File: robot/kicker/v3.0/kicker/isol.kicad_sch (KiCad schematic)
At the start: 11 parts, among them J4 Conn_01x10, U6 ISO6720-Q1, U7 ISO6720-Q1, U8 ISO6721-Q1

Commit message: kicker v3.0 digital schematic work
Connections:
- net GND_ISOL: now also R51.1; no longer R51.2
- net ~{DET}: now also R51.2; no longer R51.1
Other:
- note removed: "This power management IC is isolated from HV side."
- moved on the sheet: C, C43, C44, C45, C46, C47, J4, R51, U6, U7, U8

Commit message: lots of ERC work
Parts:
- renumbered C to C28, C43 to C29, C44 to C30, C45 to C31, C46 to C32, C47 to C33, R51 to R49, U6 to U9
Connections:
- net BOOT0 renamed MCU_BOOT_UART.BOOT0
- net PWR_EN renamed MCU_BOOT_UART.PWR_EN
- net RX renamed MCU_BOOT_UART.RX
- net TX renamed MCU_BOOT_UART.TX
- net ~{DET} renamed MCU_BOOT_UART.~{DET}
- net ~{RST} renamed MCU_BOOT_UART.~{RST}
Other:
- moved on the sheet: C28, C29, C30, C31, C32, C33, R49, U7, U8, U9

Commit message: kicker v3.0 passing ERC
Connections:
- net CLK_8M.CLK_n renamed 32KHZ_CLK_REF
- net CLK_8M.CLK_p renamed 8MHZ_CLK_REF
- net CLK_8M_ISOLn renamed CLK_32K_ISOL
- net CLK_8M_ISOLp renamed CLK_8M_ISOL
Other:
- company: (none) -> SSL A-Team
- title: (none) -> Kicker v3.0
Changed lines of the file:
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@@
 (kicad_sch (version 20230121) (generator eeschema)
   (paper "A4")
+  (title_block
+    (title "Kicker v3.0")
+    (date "2023-11-07")
+    (rev "0")
+    (company "SSL A-Team")
+    (comment 1 "Author: William Stuckey")
+  )
   (junction (at 223.52 113.03) (diameter 0) (color 0 0 0 0)
   )
@@
   (junction (at 173.99 113.03) (diameter 0) (color 0 0 0 0)
   )
+  (bus_entry (at 248.92 127) (size -2.54 2.54)
+    (stroke (width 0) (type default))
+  )
+  (bus_entry (at 111.76 53.34) (size -2.54 2.54)
+    (stroke (width 0) (type default))
+  )
+  (bus_entry (at 248.92 129.54) (size -2.54 2.54)
+    (stroke (width 0) (type default))
+  )
+  (bus_entry (at 248.92 83.82) (size -2.54 2.54)
+    (stroke (width 0) (type default))
+  )
+  (bus_entry (at 248.92 86.36) (size -2.54 2.54)
+    (stroke (width 0) (type default))
+  )
+  (bus_entry (at 247.65 43.18) (size -2.54 2.54)
+    (stroke (width 0) (type default))
+  )
+  (bus_entry (at 111.76 55.88) (size -2.54 2.54)
+    (stroke (width 0) (type default))
+  )
+  (bus_entry (at 111.76 55.88) (size -2.54 2.54)
+    (stroke (width 0) (type default))
+  )
   (bus_entry (at 247.65 45.72) (size -2.54 2.54)
     (stroke (width 0) (type default))
   )
-  (bus_entry (at 248.92 127) (size -2.54 2.54)
-    (stroke (width 0) (type default))
-  )
-  (bus_entry (at 111.76 53.34) (size -2.54 2.54)
-    (stroke (width 0) (type default))
-  )
-  (bus_entry (at 248.92 129.54) (size -2.54 2.54)
-    (stroke (width 0) (type default))
-  )
-  (bus_entry (at 248.92 83.82) (size -2.54 2.54)
-    (stroke (width 0) (type default))
-  )
-  (bus_entry (at 248.92 86.36) (size -2.54 2.54)
-    (stroke (width 0) (type default))
-  )
-  (bus_entry (at 111.76 55.88) (size -2.54 2.54)
-    (stroke (width 0) (type default))
-  )
-  (bus_entry (at 247.65 43.18) (size -2.54 2.54)
-    (stroke (width 0) (type default))
-  )
-  (bus_entry (at 111.76 55.88) (size -2.54 2.54)
-    (stroke (width 0) (type default))
-  )
   (wire (pts (xy 100.33 55.88) (xy 109.22 55.88))
     (stroke (width 0) (type default))
@@
     (effects (font (size 1.27 1.27)) (justify left bottom))
   )
-  (label "CLK_8M_ISOLn" (at 52.07 63.5 0) (fields_autoplaced)
+  (label "CLK_32K_ISOL" (at 52.07 63.5 0) (fields_autoplaced)
     (effects (font (size 1.27 1.27)) (justify left bottom))
   )
@@
     (effects (font (size 1.27 1.27)) (justify left bottom))
   )
-  (label "CLK_8M.CLK_n" (at 215.9 48.26 0) (fields_autoplaced)
-    (effects (font (size 1.27 1.27)) (justify left bottom))
-  )
-  (label "CLK_8M_ISOLp" (at 182.88 45.72 180) (fields_autoplaced)
+  (label "CLK_8M_ISOL" (at 182.88 45.72 180) (fields_autoplaced)
     (effects (font (size 1.27 1.27)) (justify right bottom))
   )
@@
     (effects (font (size 1.27 1.27)) (justify left bottom))
   )
-  (label "MCU_BOOT_UART.PWR_EN" (at 71.12 58.42 0)
+  (label "32KHZ_CLK_REF" (at 217.17 48.26 0)
+    (effects (font (size 1.27 1.27)) (justify left bottom))
+  )
+  (label "MCU_BOOT_UART.PWR_EN" (at 71.12 58.42 0) (fields_autoplaced)
     (effects (font (size 1.27 1.27)) (justify left bottom))
   )
@@
     (effects (font (size 1.27 1.27)) (justify right bottom))
   )
-  (label "CLK_8M.CLK_p" (at 215.9 45.72 0) (fields_autoplaced)
-    (effects (font (size 1.27 1.27)) (justify left bottom))
-  )
   (label "MCU_BOOT_UART.TX" (at 215.9 88.9 0) (fields_autoplaced)
     (effects (font (size 1.27 1.27)) (justify left bottom))
@@
     (effects (font (size 1.27 1.27)) (justify left bottom))
   )
+  (label "8MHZ_CLK_REF" (at 217.17 45.72 0)
+    (effects (font (size 1.27 1.27)) (justify left bottom))
+  )
   (label "BOOT_UART_TX_ISOL" (at 182.88 88.9 180) (fields_autoplaced)
     (effects (font (size 1.27 1.27)) (justify right bottom))
@@
     (effects (font (size 1.27 1.27)) (justify left bottom))
   )
-  (label "CLK_8M_ISOLn" (at 182.88 48.26 180) (fields_autoplaced)
+  (label "CLK_32K_ISOL" (at 182.88 48.26 180) (fields_autoplaced)
     (effects (font (size 1.27 1.27)) (justify right bottom))
   )
@@
     (effects (font (size 1.27 1.27)) (justify left bottom))
   )
-  (label "CLK_8M_ISOLp" (at 52.07 60.96 0) (fields_autoplaced)
-    (effects (font (size 1.27 1.27)) (justify left bottom))
-  )
-  (label "MCU_BOOT_UART.~{RST}" (at 214.63 132.08 0)
+  (label "CLK_8M_ISOL" (at 52.07 60.96 0) (fields_autoplaced)
+    (effects (font (size 1.27 1.27)) (justify left bottom))
+  )
+  (label "MCU_BOOT_UART.~{RST}" (at 214.63 132.08 0) (fields_autoplaced)
     (effects (font (size 1.27 1.27)) (justify left bottom))
   )
@@
     (effects (font (size 1.27 1.27)) (justify left))
   )
-  (hierarchical_label "CLK_8M{DCLK}" (shape output) (at 251.46 39.37 0) (fields_autoplaced)
+  (hierarchical_label "{SYSCLK}" (shape output) (at 251.46 39.37 0) (fields_autoplaced)
     (effects (font (size 1.27 1.27)) (justify left))
   )

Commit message: footprint work
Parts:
- C28, C29, C30, C31, C32, C33: value 100n -> 100n 6.3V
- J4: footprint (none) -> Connector_JST:JST_SH_SM10B-SRSS-TB_1x10-1MP_P1.00mm_Horizontal
- R49: footprint (none) -> Resistor_SMD:R_0402_1005Metric
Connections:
- net GND: now also C31.2, C32.2, C33.2
- net GND_ISOL: no longer C31.2, C32.2, C33.2
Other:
- moved on the sheet: C28, C29, C30, C31, C32, C33

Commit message: kicker v3.0 footprint work
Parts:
- C28, C29, C30, C31, C32, C33: footprint (none) -> Capacitor_SMD:C_0402_1005Metric
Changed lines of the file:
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@@
       (effects (font (size 1.27 1.27)) (justify left))
     )
-    (property "Footprint" "" (at 171.45 74.93 0)
+    (property "Footprint" "Capacitor_SMD:C_0402_1005Metric" (at 171.45 74.93 0)
       (effects (font (size 1.27 1.27)) hide)
     )
@@
       (effects (font (size 1.27 1.27)) (justify left))
     )
-    (property "Footprint" "" (at 226.06 72.39 0)
+    (property "Footprint" "Capacitor_SMD:C_0402_1005Metric" (at 226.06 72.39 0)
       (effects (font (size 1.27 1.27)) hide)
     )
@@
       (effects (font (size 1.27 1.27)) (justify left))
     )
-    (property "Footprint" "" (at 171.45 118.11 0)
+    (property "Footprint" "Capacitor_SMD:C_0402_1005Metric" (at 171.45 118.11 0)
       (effects (font (size 1.27 1.27)) hide)
     )
@@
       (effects (font (size 1.27 1.27)) (justify left))
     )
-    (property "Footprint" "" (at 226.06 115.57 0)
+    (property "Footprint" "Capacitor_SMD:C_0402_1005Metric" (at 226.06 115.57 0)
       (effects (font (size 1.27 1.27)) hide)
     )
@@
       (effects (font (size 1.27 1.27)) (justify left))
     )
-    (property "Footprint" "" (at 170.18 34.29 0)
+    (property "Footprint" "Capacitor_SMD:C_0402_1005Metric" (at 170.18 34.29 0)
       (effects (font (size 1.27 1.27)) hide)
     )
@@
       (effects (font (size 1.27 1.27)) (justify left))
     )
-    (property "Footprint" "" (at 227.33 31.75 0)
-      (effects (font (size 1.27 1.27)) hide)
-    )
+    (property "Footprint" "Capacitor_SMD:C_0402_1005Metric" (at 227.33 31.75 0)
+      (effects (font (size 1.27 1.27)) hide)
+    )

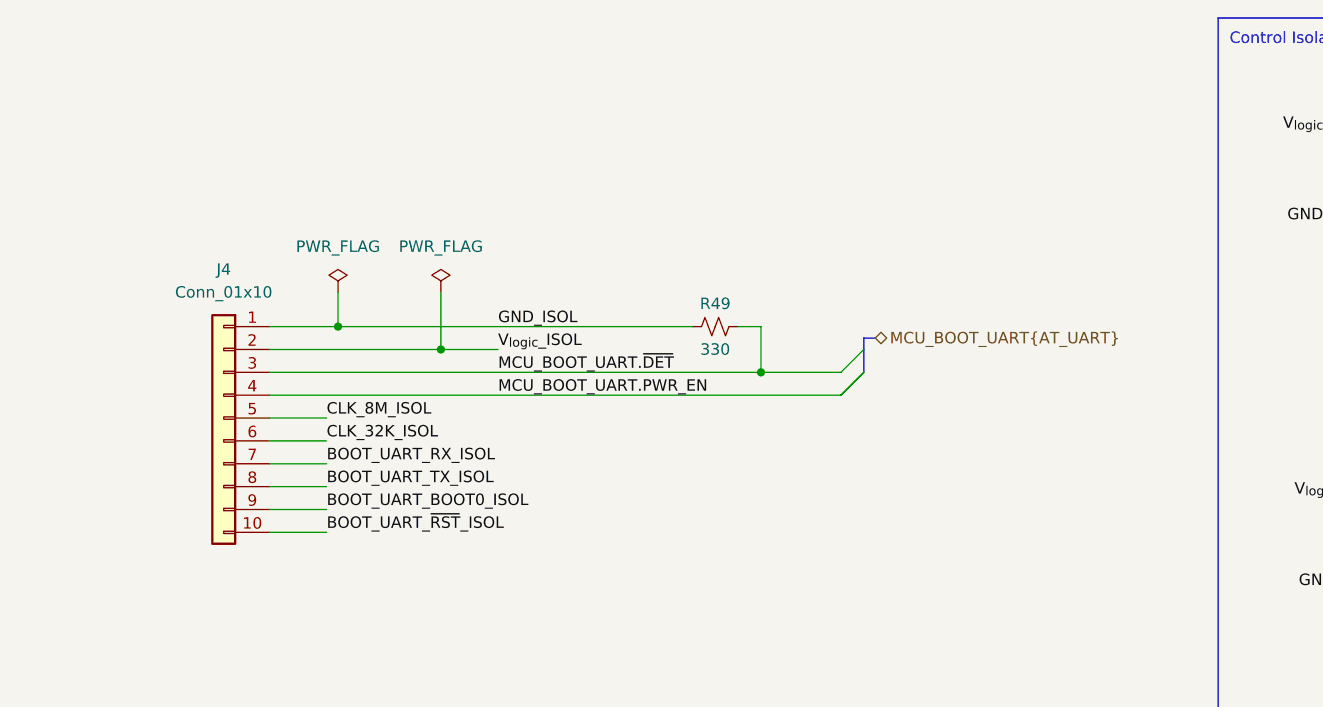
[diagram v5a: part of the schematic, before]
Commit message: kicker v3.0 footprint work
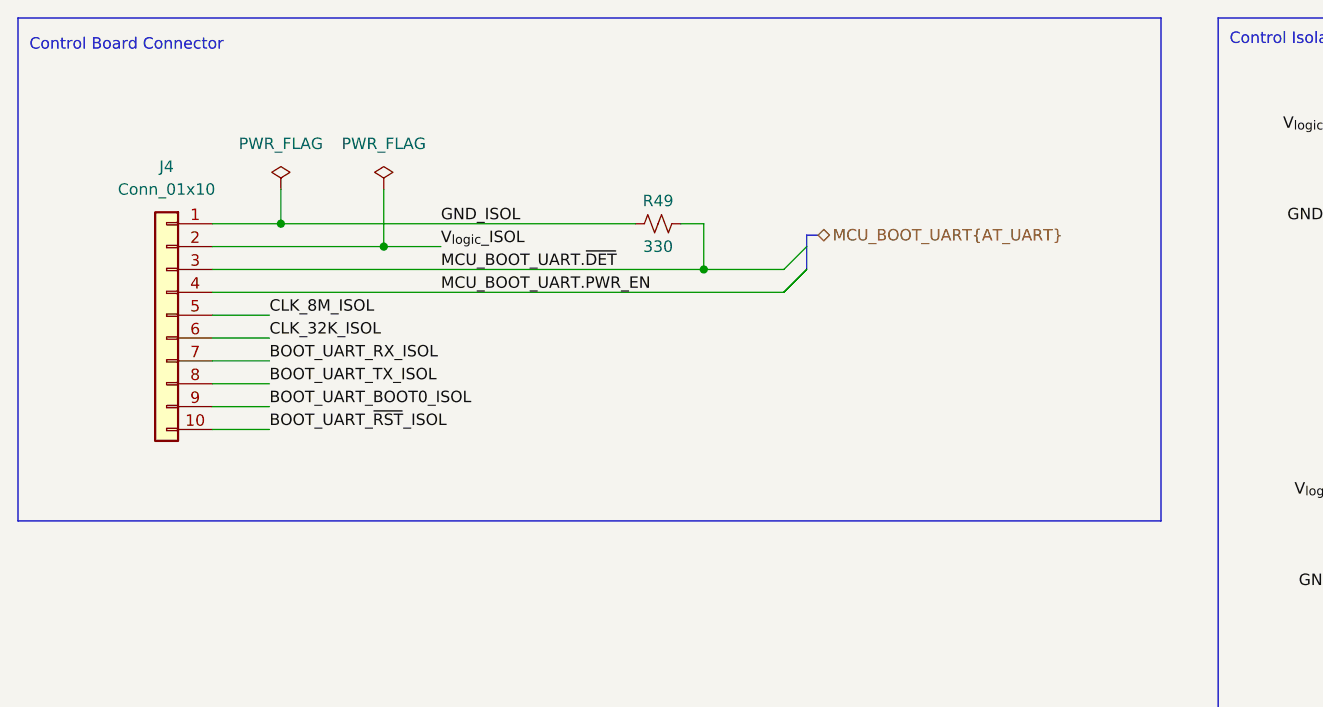
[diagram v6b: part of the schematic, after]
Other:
- note added: "Control Board Connector"
- moved on the sheet: J4, R49

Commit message: kicker v3.0 footprint work
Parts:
- U7, U8, U9: footprint (none) -> AT-IC:ISO672X
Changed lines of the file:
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@@
       (effects (font (size 1.27 1.27)))
     )
-    (property "Footprint" "" (at 199.39 46.99 0)
+    (property "Footprint" "AT-IC:ISO672X" (at 199.39 46.99 0)
       (effects (font (size 1.27 1.27)) hide)
     )
@@
       (effects (font (size 1.27 1.27)))
     )
-    (property "Footprint" "" (at 199.39 87.63 0)
+    (property "Footprint" "AT-IC:ISO672X" (at 199.39 87.63 0)
       (effects (font (size 1.27 1.27)) hide)
     )
@@
       (effects (font (size 1.27 1.27)))
     )
-    (property "Footprint" "" (at 199.39 130.81 0)
-      (effects (font (size 1.27 1.27)) hide)
-    )
+    (property "Footprint" "AT-IC:ISO672X" (at 199.39 130.81 0)
+      (effects (font (size 1.27 1.27)) hide)
+    )

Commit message: kicker v3.0 ready for review
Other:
- note added: "!!IMPORTANT!!: Use ISO672X "F" variants to ensure all output logic levels are "false" when the control board is unplugged"
- note added: ""MOSI" pin 7, "MISO" pin 8"
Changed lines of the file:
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@@
     (fill (type none))
+  )
+  (text "\"MOSI\" pin 7, \"MISO\" pin 8" (at 72.39 55.88 0)
+    (effects (font (size 1.27 1.27)) (justify left bottom))
   )
   (text "Control Board Connector" (at 19.05 20.32 0)
     (effects (font (size 1.27 1.27)) (justify left bottom))
   )
+  (text "!!IMPORTANT!!: Use ISO672X \"F\" variants to ensure all output logic levels are \"false\" when the control board is unplugged"
+    (at 156.21 151.13 0)
+    (effects (font (size 1.27 1.27)) (justify left bottom))
+  )
